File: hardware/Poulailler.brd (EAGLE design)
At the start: 55.9 x 54.3 mm, 26 parts

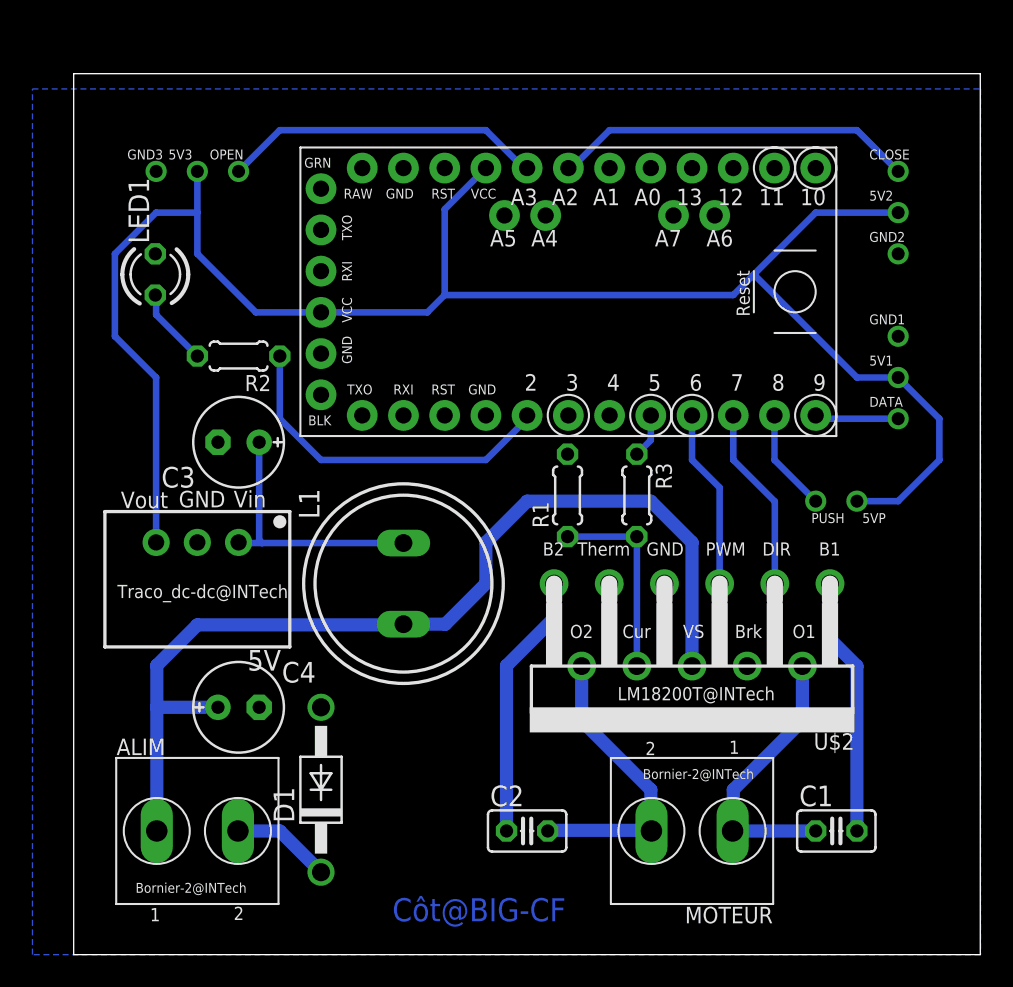
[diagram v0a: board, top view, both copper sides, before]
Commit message: réattribution de pins
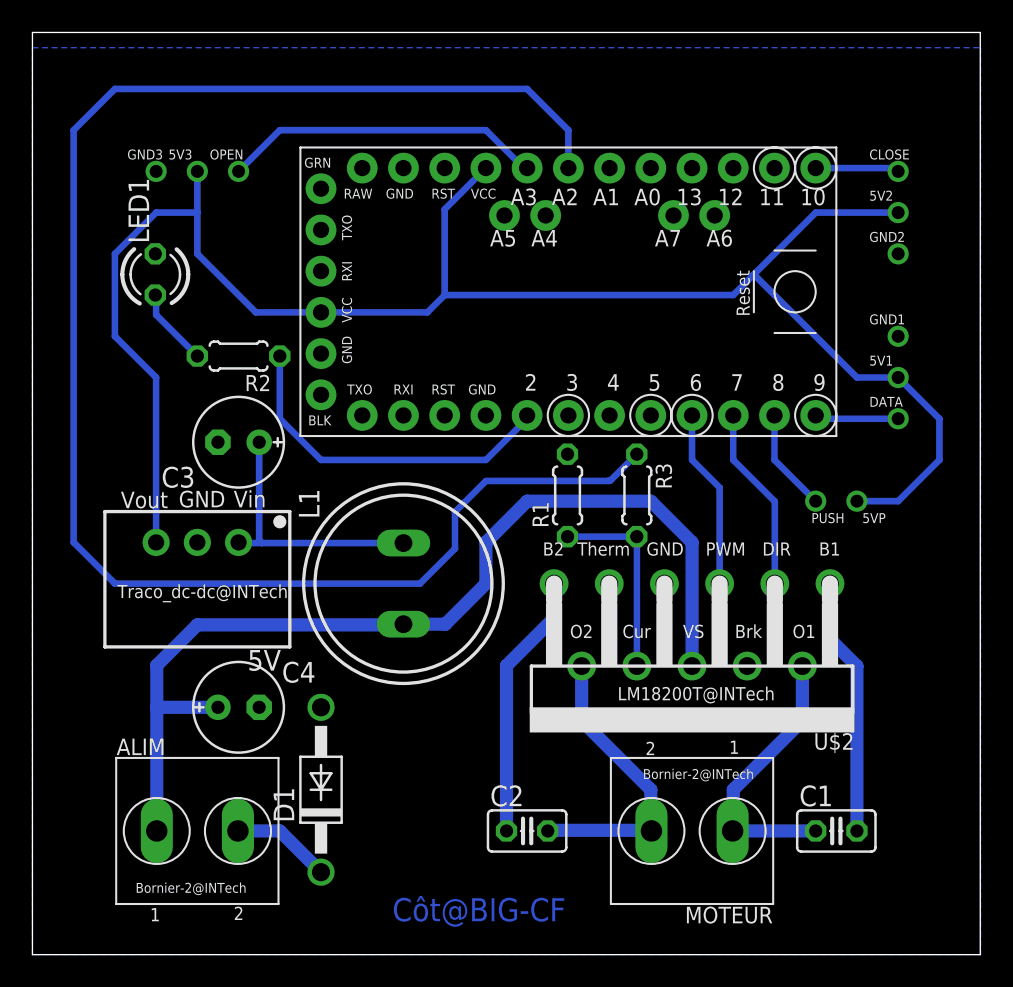
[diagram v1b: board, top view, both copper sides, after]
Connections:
- net CLOSE: now also U$1.10; no longer U$1.A2
- net SENSE: now also U$1.A2; no longer U$1.5
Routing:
- net SENSE: track 2.75 -> 100.7 mm
- net CLOSE: track 22.3 -> 5.28 mm
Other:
- board size 55.9 x 54.3 mm -> 58.4 x 56.8 mm
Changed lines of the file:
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@@
 <board>
 <plain>
-<wire x1="35.56" y1="-2.54" x2="91.42" y2="-2.54" width="0" layer="20"/>
-<wire x1="91.42" y1="-2.54" x2="91.42" y2="51.74" width="0" layer="20"/>
-<wire x1="91.42" y1="51.74" x2="35.56" y2="51.74" width="0" layer="20"/>
-<wire x1="35.56" y1="51.74" x2="35.56" y2="-2.54" width="0" layer="20"/>
-<dimension x1="35.56" y1="-2.54" x2="35.56" y2="51.7144" x3="25.4" y3="24.5872" layer="20"/>
-<dimension x1="35.56" y1="51.74" x2="91.42" y2="51.74" x3="63.49" y3="55.880003125" layer="20"/>
+<wire x1="33.02" y1="-2.54" x2="91.42" y2="-2.54" width="0" layer="20"/>
+<wire x1="91.42" y1="-2.54" x2="91.42" y2="54.28" width="0" layer="20"/>
+<wire x1="91.42" y1="54.28" x2="33.02" y2="54.28" width="0" layer="20"/>
+<wire x1="33.02" y1="54.28" x2="33.02" y2="-2.54" width="0" layer="20"/>
+<dimension x1="33.02" y1="-2.54" x2="33.02" y2="54.2544" x3="22.86" y3="25.8572" layer="20"/>
+<dimension x1="33.02" y1="54.28" x2="91.42" y2="54.28" x3="62.22" y3="58.420003125" layer="20"/>
 <text x="65.8876" y="0.9398" size="1.4224" layer="16" font="vector" rot="R180">Côt@BIG-CF</text>
 </plain>
@@
 <contactref element="U$2" pad="4"/>
 <polygon width="0.4064" layer="16">
-<vertex x="33.02" y="50.8"/>
-<vertex x="91.44" y="50.8"/>
+<vertex x="33.02" y="53.34"/>
+<vertex x="91.44" y="53.34"/>
 <vertex x="91.44" y="-2.54"/>
 <vertex x="33.02" y="-2.54"/>
@@
 </signal>
 <signal name="CLOSE">
-<contactref element="U$1" pad="A2"/>
 <contactref element="CLOSE" pad="DATA"/>
-<wire x1="66.04" y1="45.9232" x2="66.2432" y2="45.9232" width="0.4064" layer="16"/>
-<wire x1="66.2432" y1="45.9232" x2="68.58" y2="48.26" width="0.4064" layer="16"/>
-<wire x1="68.58" y1="48.26" x2="83.82" y2="48.26" width="0.4064" layer="16"/>
-<wire x1="83.82" y1="48.26" x2="86.36" y2="45.72" width="0.4064" layer="16"/>
+<contactref element="U$1" pad="10"/>
+<wire x1="81.28" y1="45.9232" x2="86.36" y2="45.9232" width="0.4064" layer="16"/>
+<wire x1="86.36" y1="45.9232" x2="86.36" y2="45.72" width="0.4064" layer="16"/>
 </signal>
 <signal name="OPEN">
@@
 </signal>
 <signal name="SENSE">
-<contactref element="U$1" pad="5"/>
 <contactref element="R3" pad="1"/>
-<wire x1="70.2564" y1="28.2956" x2="71.12" y2="29.1592" width="0.4064" layer="16"/>
-<wire x1="71.12" y1="29.1592" x2="71.12" y2="30.6832" width="0.4064" layer="16"/>
+<contactref element="U$1" pad="A2"/>
+<wire x1="70.2564" y1="28.2956" x2="68.6308" y2="26.67" width="0.4064" layer="16"/>
+<wire x1="68.6308" y1="26.67" x2="68.5546" y2="26.67" width="0.4064" layer="16"/>
+<wire x1="68.5546" y1="26.67" x2="68.5292" y2="26.6446" width="0.4064" layer="16"/>
+<wire x1="68.5292" y1="26.6446" x2="60.96" y2="26.6446" width="0.4064" layer="16"/>
+<wire x1="59.055" y1="22.479" x2="56.896" y2="20.32" width="0.4064" layer="16"/>
+<wire x1="56.896" y1="20.32" x2="38.1" y2="20.32" width="0.4064" layer="16"/>
+<wire x1="35.56" y1="22.86" x2="35.56" y2="48.26" width="0.4064" layer="16"/>
+<wire x1="35.56" y1="48.26" x2="38.1" y2="50.8" width="0.4064" layer="16"/>
+<wire x1="38.1" y1="50.8" x2="63.5" y2="50.8" width="0.4064" layer="16"/>
+<wire x1="63.5" y1="50.8" x2="66.04" y2="48.26" width="0.4064" layer="16"/>
+<wire x1="66.04" y1="48.26" x2="66.04" y2="45.9232" width="0.4064" layer="16"/>
+<wire x1="59.055" y1="22.479" x2="59.055" y2="24.7396" width="0.4064" layer="16"/>
+<wire x1="59.055" y1="24.7396" x2="60.96" y2="26.6446" width="0.4064" layer="16"/>
+<wire x1="38.1" y1="20.32" x2="35.56" y2="22.86" width="0.4064" layer="16"/>
 </signal>
 <signal name="N$4">
@@
 </signal>
 </signals>
-<errors>
-</errors>
 </board>
 </drawing>
